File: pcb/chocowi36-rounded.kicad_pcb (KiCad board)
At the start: 2 copper layers, 113.1 x 88.3 mm, 27 parts, among them SW10 SW_Push, SW11 SW_Push, SW12 SW_Push, SW14 SW_Push, SW15 SW_Push, SW16 SW_Push, SW17 SW_Push, SW18 SW_Push, SW19 SW_Push, SW2 SW_Push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

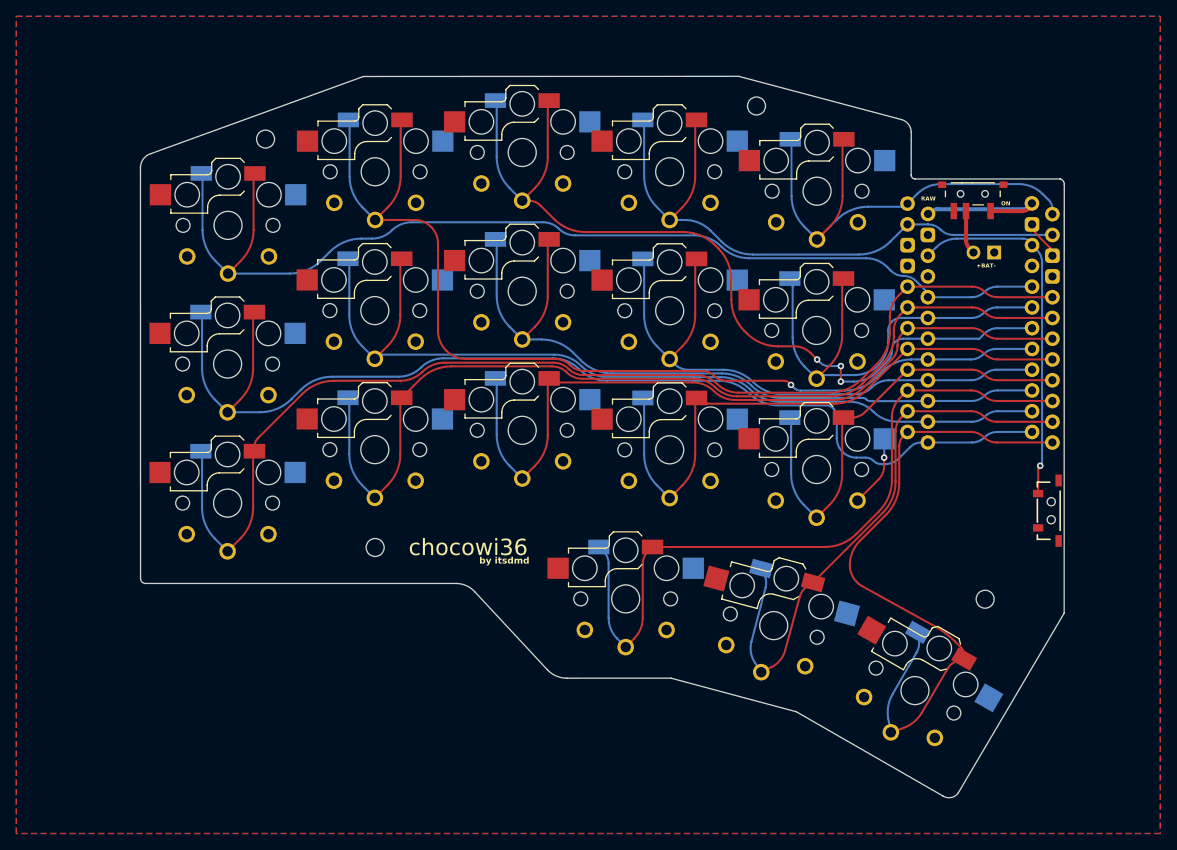
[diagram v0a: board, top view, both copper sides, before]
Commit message: adjust thumb cluster
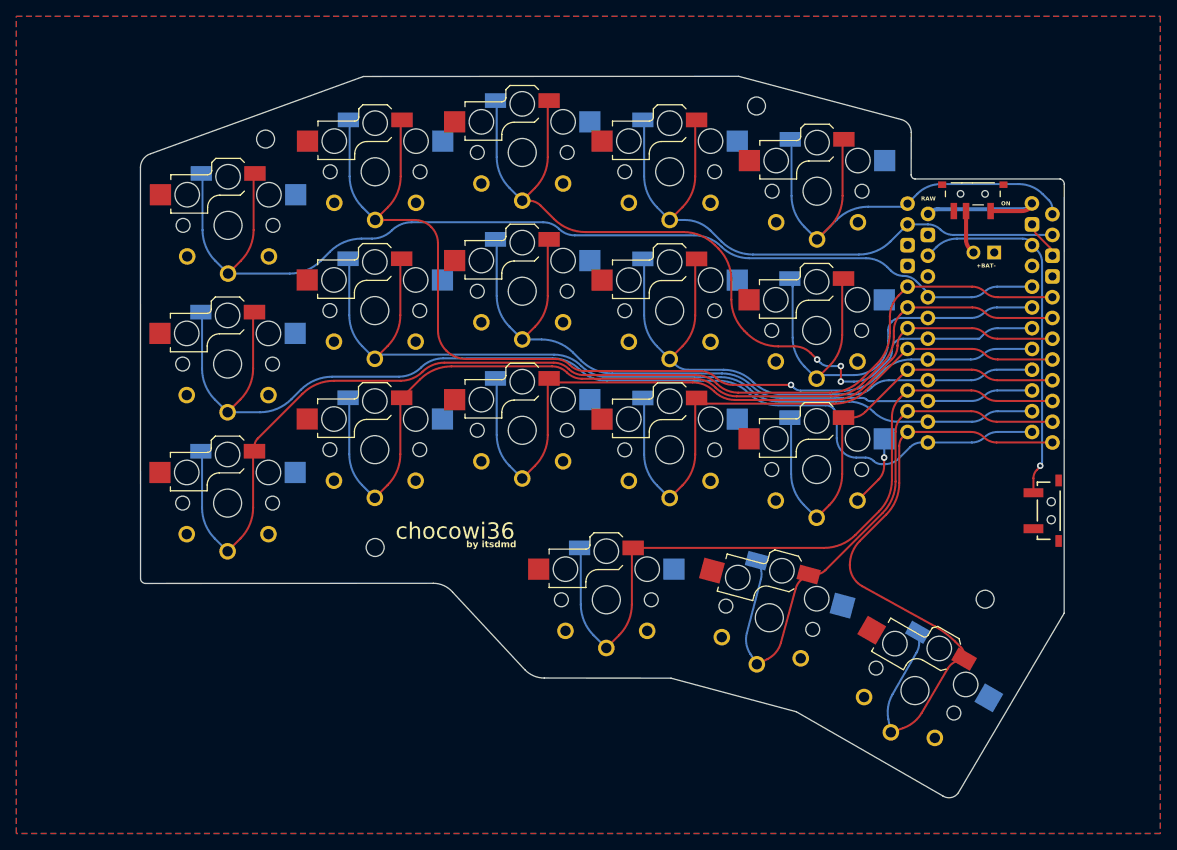
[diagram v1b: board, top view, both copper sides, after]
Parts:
- moved SW19 2.37 mm to (132.2, 111.4)
- moved SW20 1.11 mm to (152.1, 113.6)
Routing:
- net Switch19: track 89.8 -> 92.3 mm
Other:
- outline, holes or cut-outs redrawn

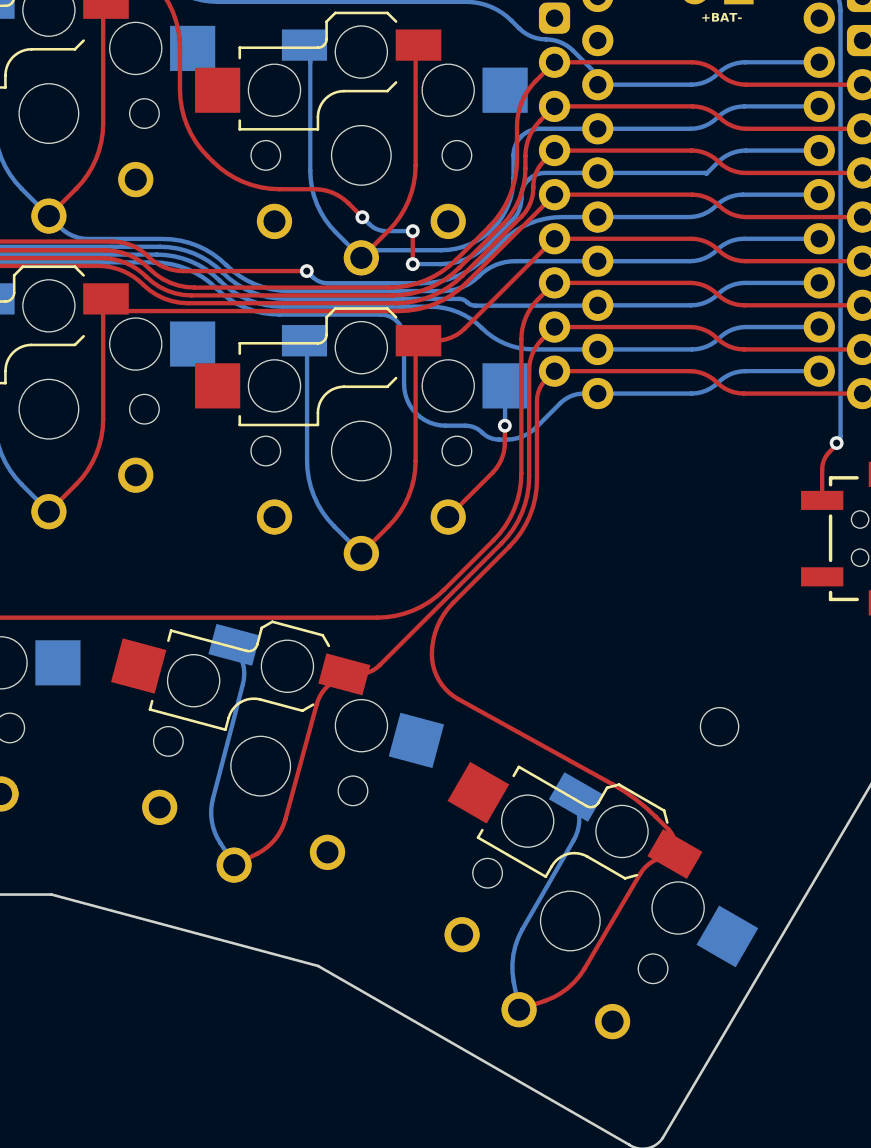
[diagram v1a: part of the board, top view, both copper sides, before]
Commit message: fix thumb cluster
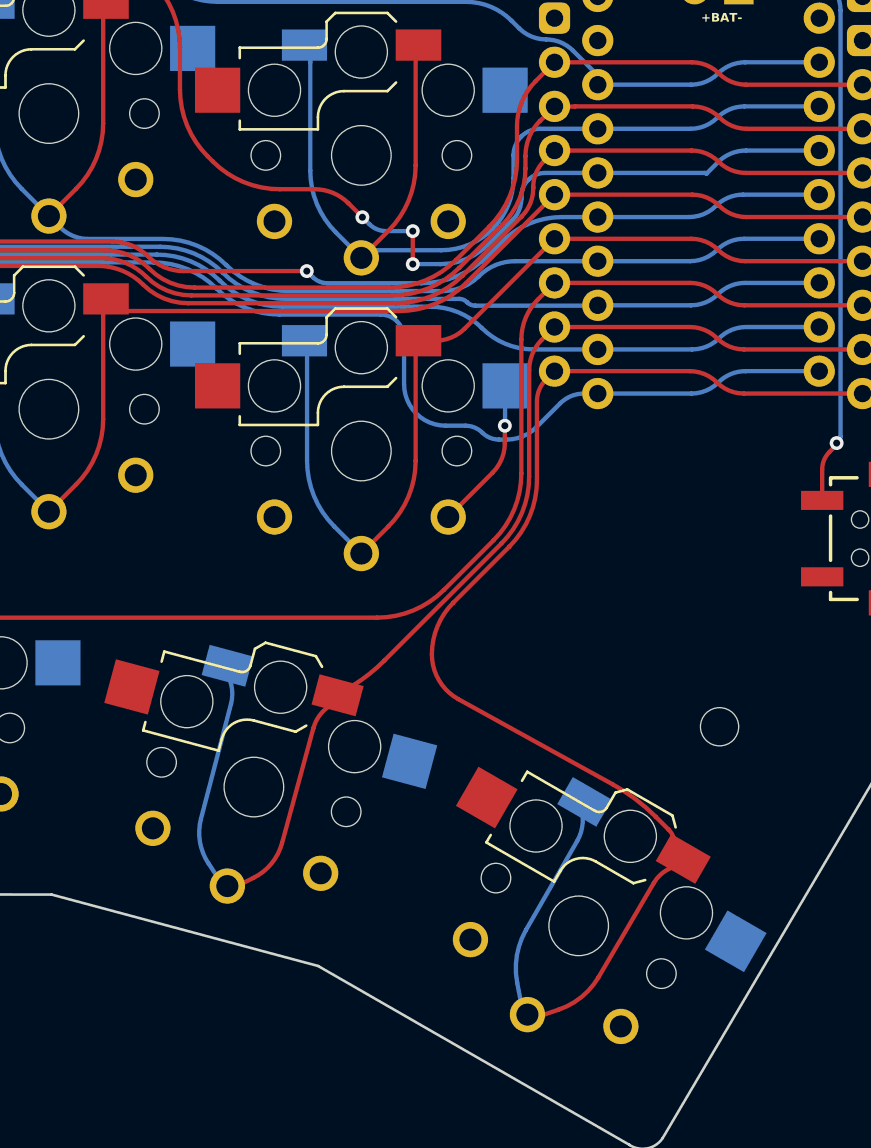
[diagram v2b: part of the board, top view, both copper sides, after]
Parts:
- moved SW20 1.27 mm to (151.8, 114.8)
- moved SW21 0.56 mm to (170.4, 122.8)
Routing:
- net Switch20: track 70.2 -> 71.0 mm

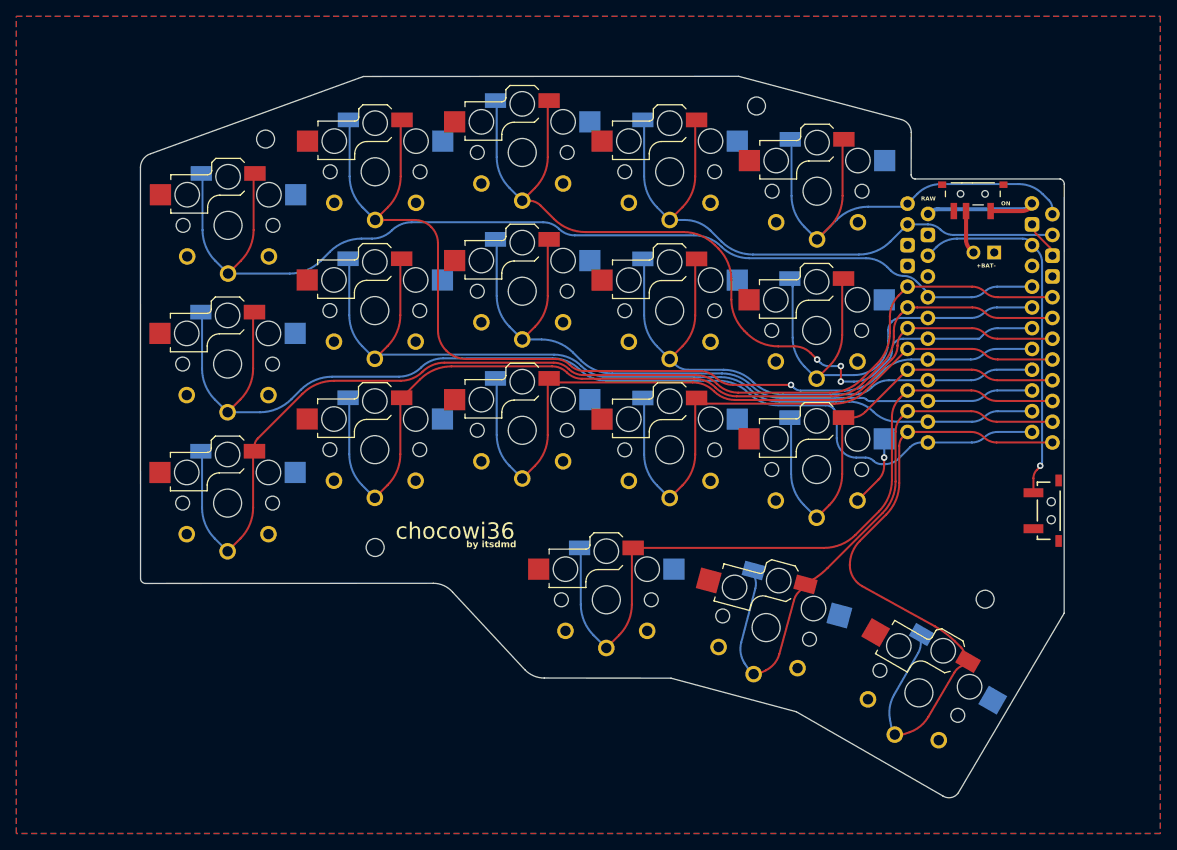
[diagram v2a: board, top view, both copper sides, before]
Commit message: update routing to support placing tactile switches on both sides
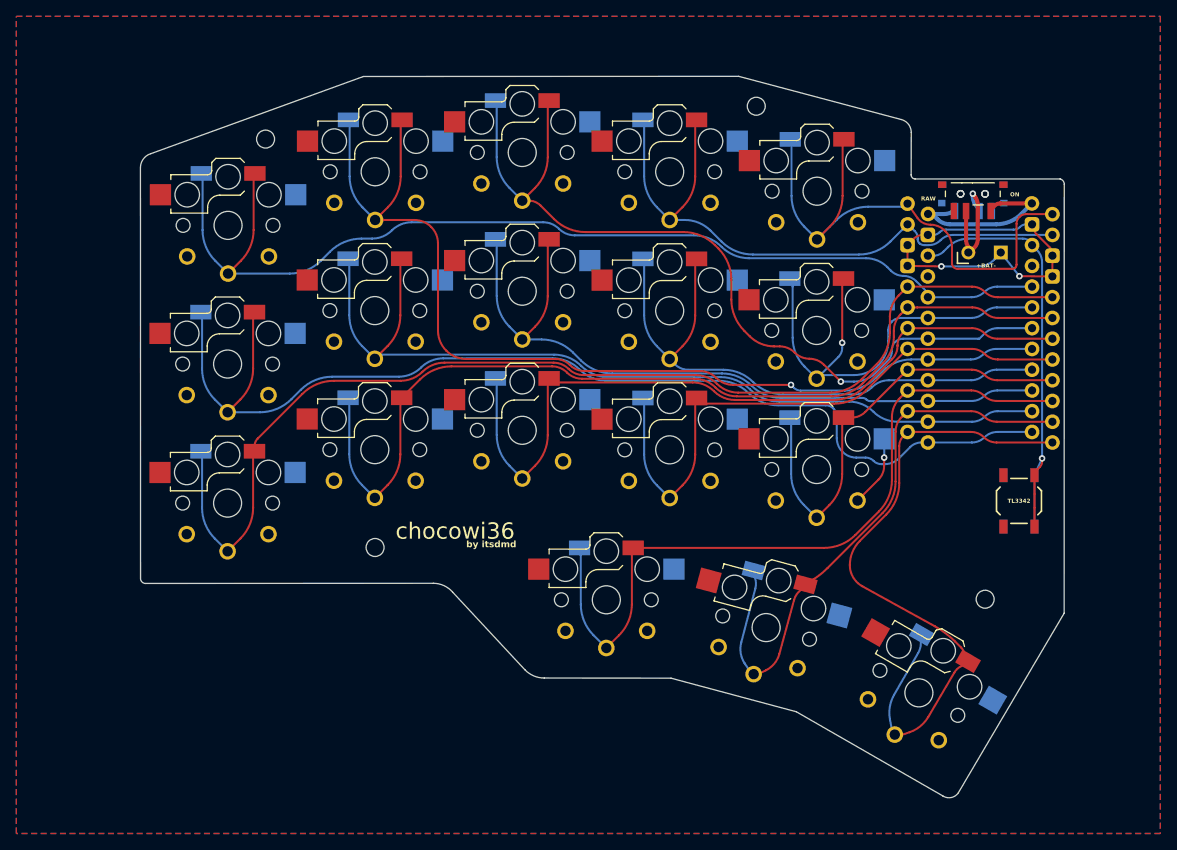
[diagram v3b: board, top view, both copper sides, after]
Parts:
- removed ? (x2): , 
- added H2: MountingHole, itsdmd:MountingHole_2.2mm_M2, F.Cu at (103.9, 105.0)
- added H3: MountingHole, itsdmd:MountingHole_2.2mm_M2, F.Cu at (150.6, 51.0)
- added SW_POWER2: SW_SPDT, itsdmd:SW-S_MSK-12C02, B.Cu at (176.9, 61.7)
- added SW_RST2: SW_Push, itsdmd:SW-T_SPST_TL3342, B.Cu at (182.7, 99.3)
- SW_RST1: footprint itsdmd:SW-T_7.4x2.6-4pad-smd -> itsdmd:SW-T_SPST_TL3342
- moved SW_RST1 4.22 mm to (182.7, 99.3)
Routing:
- net gnd: track 15.0 -> 55.0 mm, vias 1 -> 3
- net reset: track 45.0 -> 57.4 mm
- net Net-(BT1-+): track 5.37 -> 15.5 mm, vias 0 -> 1
- net Switch6: track 59.8 -> 68.0 mm
- net +BATT: track 19.0 -> 22.3 mm
- net Switch5: track 76.1 -> 77.4 mm
- net Switch4: track 103.9 -> 102.7 mm, vias 3 -> 1
- net Switch19: track 92.3 -> 93.5 mm
- net Switch12: track 57.5 -> 57.8 mm, vias 0 -> 1
